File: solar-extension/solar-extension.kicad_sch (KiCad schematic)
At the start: 3 parts, among them J3 302-S201

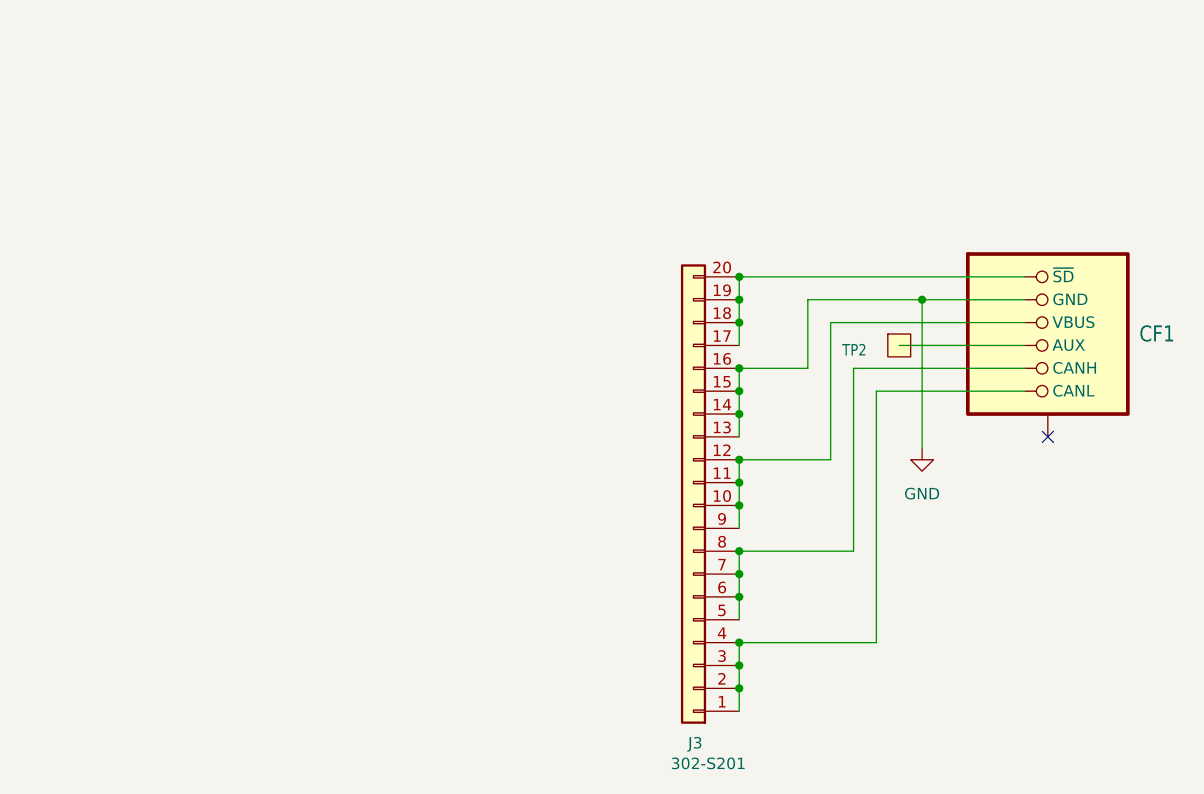
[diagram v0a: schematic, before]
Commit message: solar extension board finished !
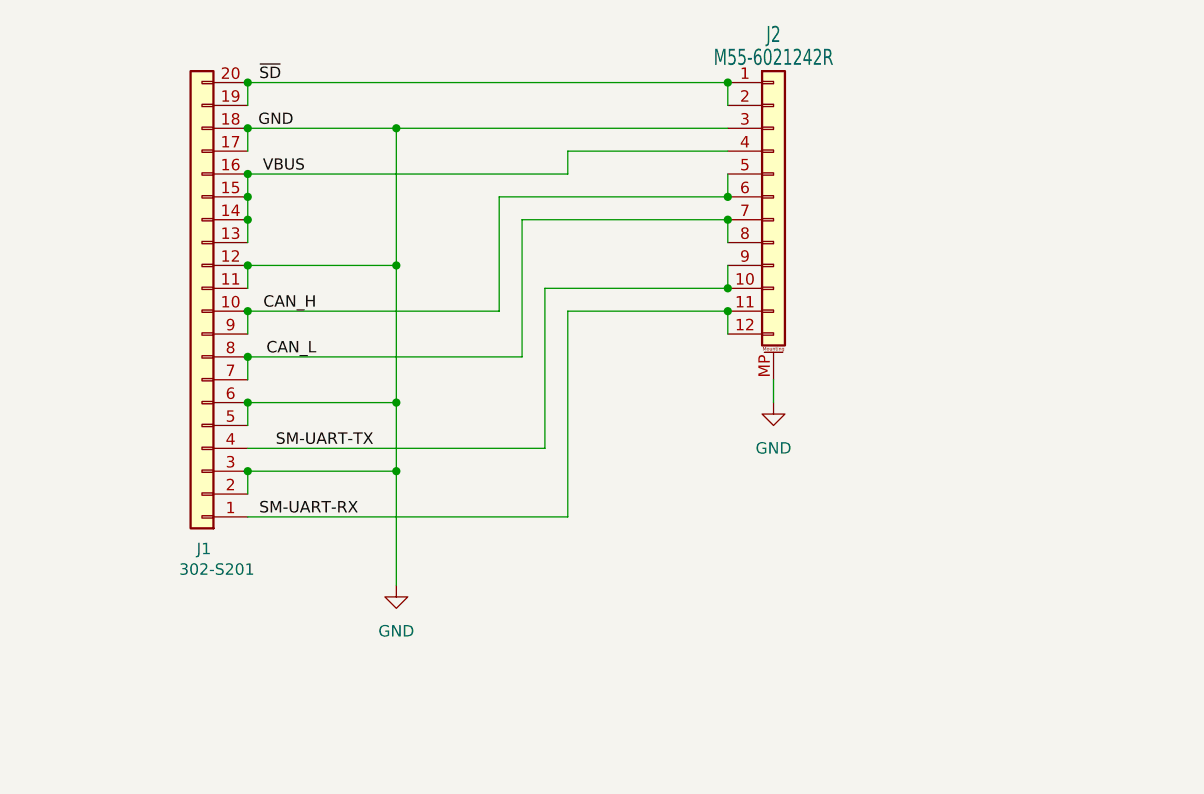
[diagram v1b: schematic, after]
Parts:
- removed CF1: (no value), oresat-connectors:J-Harwin-M55-60X1242R, symbol oresat-connectors:M55-6021242R
- removed J3: 302-S201, Connector_IDC:IDC-Header_2x10_P2.54mm_Vertical, symbol Connector_Generic:Conn_01x20
- removed TP2: TEST-POINT-LARGE-SQUARE, oresat-misc:TestPoint_Pad_D1.0mm, symbol oresat-misc:Test-Point-0.75mm-th
- added J1: 302-S201, Connector_IDC:IDC-Header_2x10_P2.54mm_Vertical, symbol Connector_Generic:Conn_01x20
- added J2: M55-6021242R, oresat-connectors:J-Harwin-M55-60X1242R, symbol Connector_Generic_MountingPin:Conn_01x12_MountingPin
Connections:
- net GND: now also J1.11 (Pin_11), J1.12 (Pin_12), J1.17 (Pin_17), J1.18 (Pin_18), J1.2 (Pin_2), J1.3 (Pin_3), J1.5 (Pin_5), J1.6 (Pin_6), J2.3 (Pin_3), J2.MP (MountPin)
- new net CAN_H: J1.10 (Pin_10), J1.9 (Pin_9), J2.5 (Pin_5), J2.6 (Pin_6)
- new net CAN_L: J1.7 (Pin_7), J1.8 (Pin_8), J2.7 (Pin_7), J2.8 (Pin_8)
- new net SM-UART-RX: J1.1 (Pin_1), J2.11 (Pin_11), J2.12 (Pin_12)
- new net SM-UART-TX: J1.4 (Pin_4), J2.10 (Pin_10), J2.9 (Pin_9)
- new net VBUS: J1.13 (Pin_13), J1.14 (Pin_14), J1.15 (Pin_15), J1.16 (Pin_16), J2.4 (Pin_4)
- new net ~{SD}: J1.19 (Pin_19), J1.20 (Pin_20), J2.1 (Pin_1), J2.2 (Pin_2)
- no-connect marks 1 -> 0
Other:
- company: oresat! -> Julia Al-Otoom
- title: 1u Solar Breakout -> Solar Extension

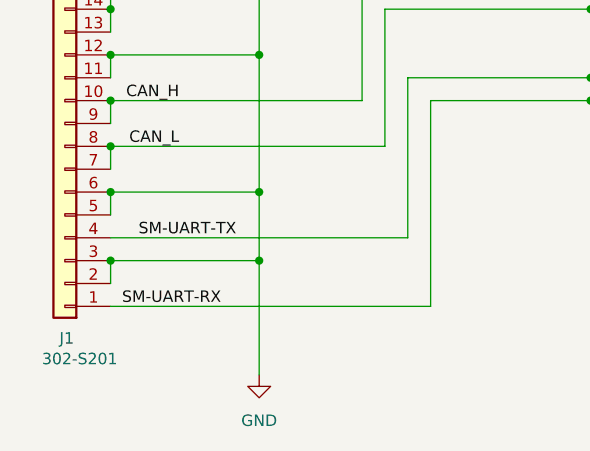
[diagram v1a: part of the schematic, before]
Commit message: final changes made to sizing after design review
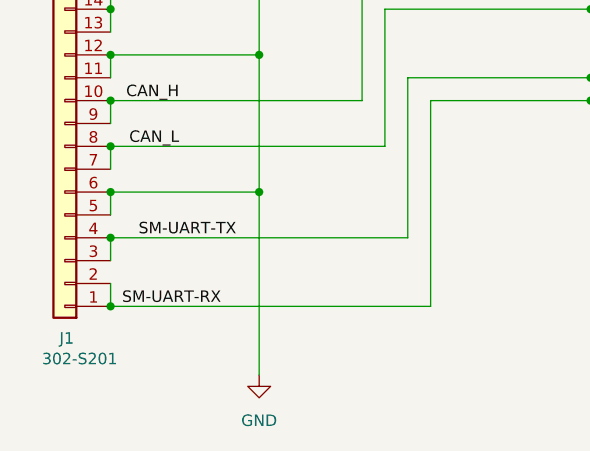
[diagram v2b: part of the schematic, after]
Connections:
- net GND: no longer J1.2 (Pin_2), J1.3 (Pin_3)
- net SM-UART-RX: now also J1.2 (Pin_2)
- net SM-UART-TX: now also J1.3 (Pin_3)
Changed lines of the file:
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@@
+	)
+	(junction
+		(at 119.38 90.17)
+		(diameter 0)
+		(color 0 0 0 0)
 	)
 	(junction
@@
 	)
 	(junction
-		(at 119.38 85.09)
-		(diameter 0)
-		(color 0 0 0 0)
-	)
-	(junction
 		(at 119.38 54.61)
 		(diameter 0)
@@
 	)
 	(junction
-		(at 135.89 85.09)
+		(at 119.38 77.47)
+		(diameter 0)
+		(color 0 0 0 0)
+	)
+	(junction
+		(at 119.38 82.55)
 		(diameter 0)
 		(color 0 0 0 0)
@@
 		(color 0 0 0 0)
 	)
-	(junction
-		(at 119.38 77.47)
-		(diameter 0)
-		(color 0 0 0 0)
-	)
 	(wire
 		(pts
@@
 	(wire
 		(pts
-			(xy 119.38 85.09) (xy 135.89 85.09)
-		)
-		(stroke
-			(width 0)
-			(type default)
-		)
-	)
-	(wire
-		(pts
 			(xy 147.32 54.61) (xy 172.72 54.61)
 		)
@@
 	(wire
 		(pts
-			(xy 119.38 87.63) (xy 119.38 85.09)
-		)
-		(stroke
-			(width 0)
-			(type default)
-		)
-	)
-	(wire
-		(pts
 			(xy 119.38 67.31) (xy 147.32 67.31)
 		)
@@
 	(wire
 		(pts
+			(xy 119.38 82.55) (xy 119.38 85.09)
+		)
+		(stroke
+			(width 0)
+			(type default)
+		)
+	)
+	(wire
+		(pts
 			(xy 119.38 82.55) (xy 152.4 82.55)
 		)
@@
 	(wire
 		(pts
+			(xy 119.38 87.63) (xy 119.38 90.17)
+		)
+		(stroke
+			(width 0)
+			(type default)
+		)
+	)
+	(wire
+		(pts
 			(xy 147.32 54.61) (xy 147.32 67.31)
 		)
@@
 	(wire
 		(pts
-			(xy 119.38 80.01) (xy 119.38 77.47)
-		)
-		(stroke
-			(width 0)
-			(type default)
-		)
-	)
-	(wire
-		(pts
 			(xy 119.38 46.99) (xy 119.38 49.53)
 		)
@@
 	(wire
 		(pts
-			(xy 135.89 97.79) (xy 135.89 85.09)
+			(xy 135.89 77.47) (xy 135.89 97.79)
 		)
 		(stroke
@@
 	(wire
 		(pts
+			(xy 119.38 77.47) (xy 119.38 80.01)
+		)
+		(stroke
+			(width 0)
+			(type default)
+		)
+	)
+	(wire
+		(pts
 			(xy 149.86 57.15) (xy 149.86 72.39)
 		)
@@
 		)
 		(stroke
-			(width 0)
-			(type default)
-		)
-	)
-	(wire
-		(pts
-			(xy 135.89 85.09) (xy 135.89 77.47)
-		)
-		(stroke

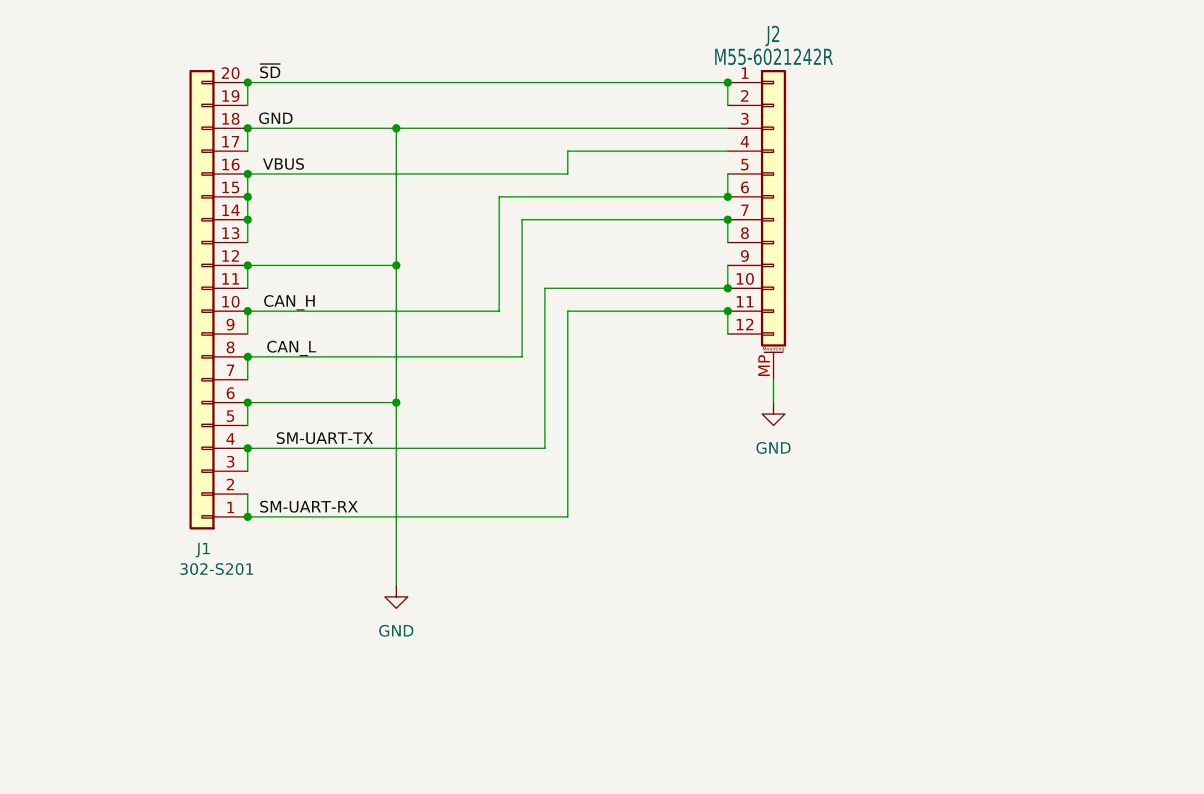
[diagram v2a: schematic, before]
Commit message: final final changes made to pinout, track width, and added vias
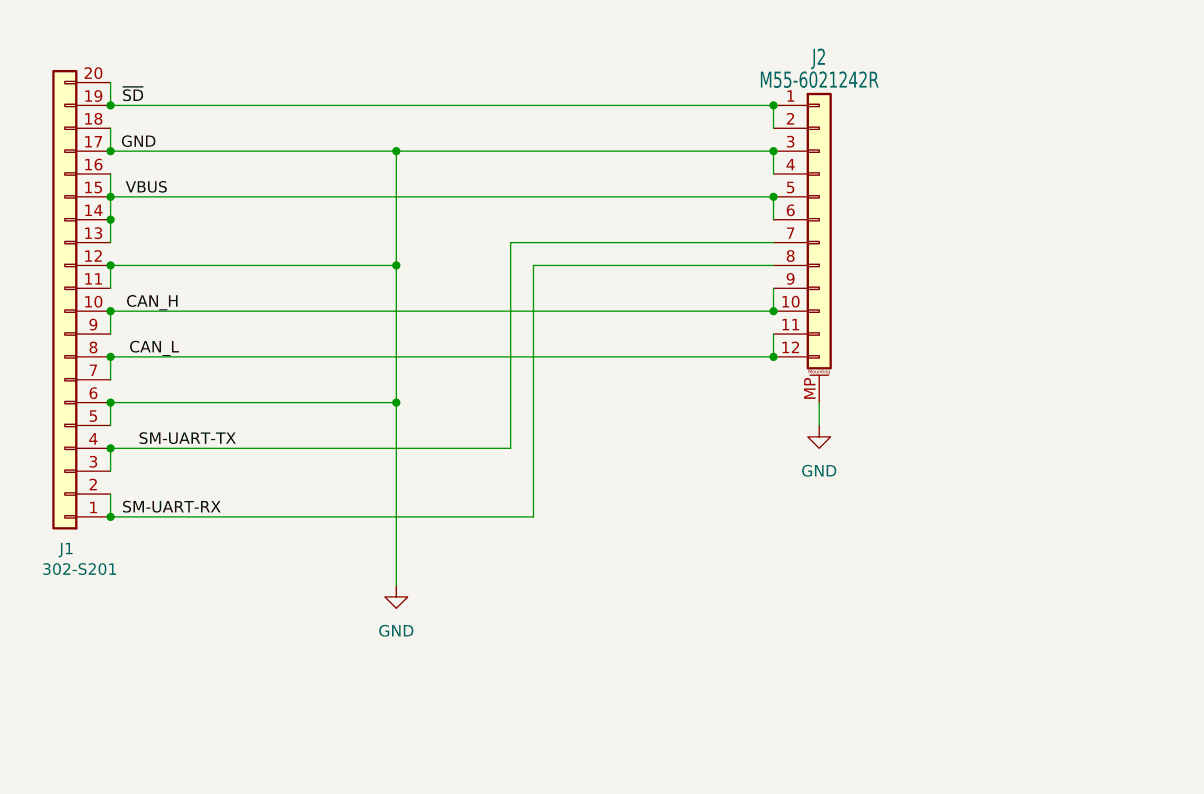
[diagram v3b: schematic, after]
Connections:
- net CAN_H: now also J2.10 (Pin_10), J2.9 (Pin_9); no longer J2.5 (Pin_5), J2.6 (Pin_6)
- net CAN_L: now also J2.11 (Pin_11), J2.12 (Pin_12); no longer J2.7 (Pin_7), J2.8 (Pin_8)
- net GND: now also J2.4 (Pin_4)
- net SM-UART-RX: now also J2.8 (Pin_8); no longer J2.11 (Pin_11), J2.12 (Pin_12)
- net SM-UART-TX: now also J2.7 (Pin_7); no longer J2.10 (Pin_10), J2.9 (Pin_9)
- net VBUS: now also J2.5 (Pin_5), J2.6 (Pin_6); no longer J2.4 (Pin_4)
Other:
- moved on the sheet: J1

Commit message: minor polishing and imported 2 layer OSH Park design rules.
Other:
- company: Julia Al-Otoom -> Portland State Aerospace Society
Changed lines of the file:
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@@
 	(title_block
 		(title "Solar Extension")
-		(date "2026-09-29")
+		(date "2026-10-02")
 		(rev "1")
-		(company "Julia Al-Otoom")
+		(company "Portland State Aerospace Society")
 	)
 	(junction
